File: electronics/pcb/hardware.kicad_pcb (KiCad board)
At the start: 4 copper layers, 59 x 53 mm, 145 parts, among them J1 Micro_SD_Card_Det_Hirose_DM3AT, J2 USB_A, J3 USB_A, J5 Conn_02x10_Odd_Even, U1 AS4C512M16D3L-12BIN, U2 A33, U3 TPS62095RGTR, U4 TPS62095RGTR, U5 TPS62095RGTR, U6 TPS62095RGTR, U7 AP131-25, Y1 24Mhz, Y2 32.768khz

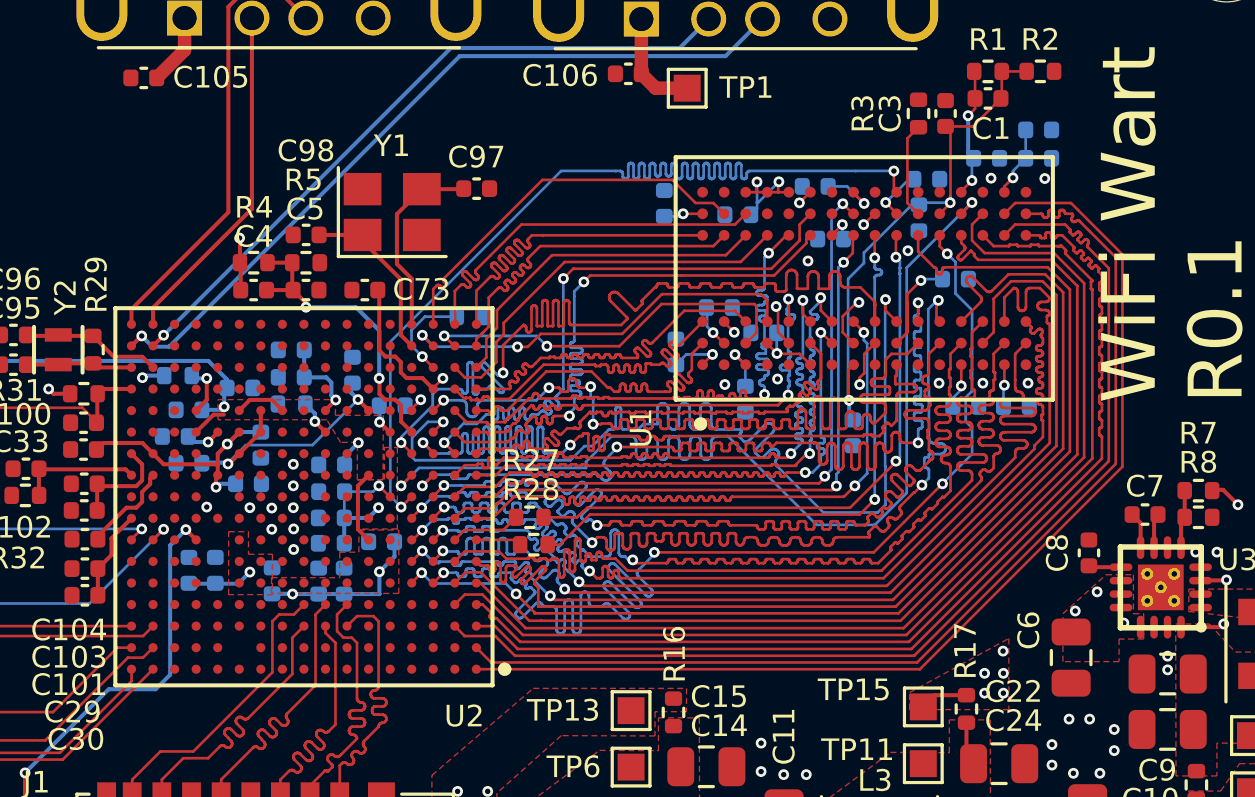
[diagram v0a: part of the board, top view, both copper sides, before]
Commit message: Working on the length matching
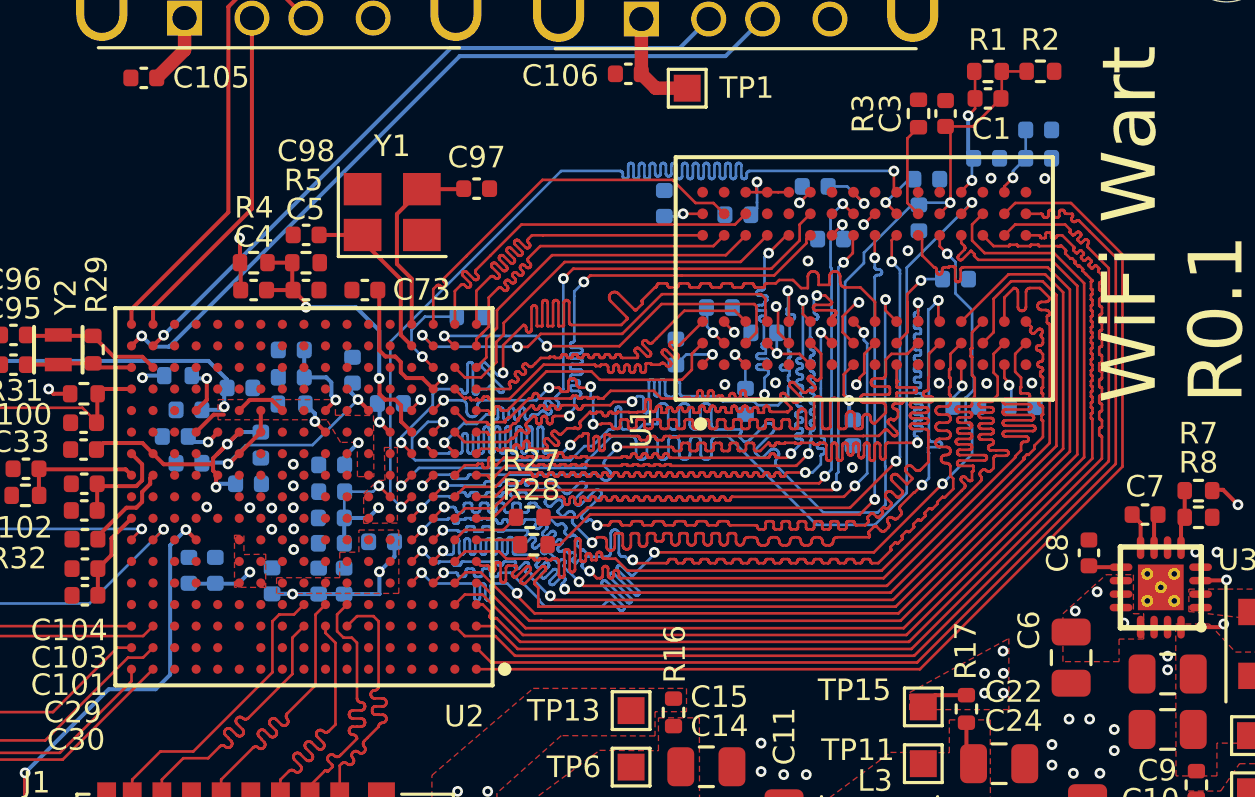
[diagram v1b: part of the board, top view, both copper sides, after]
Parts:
- moved C89 0.21 mm to (141.4, 105.6)
- moved C37 0.11 mm to (118.0, 105.5)
- moved C86 0.08 mm to (131.1, 105.4)
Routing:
- net adr15: track 48.5 -> 40.3 mm
- net d0: track 18.5 -> 24.1 mm
- net d2: track 19.7 -> 25.0 mm
- net d13: track 14.1 -> 10.4 mm
- net /ram/!RST: track 37.4 -> 40.3 mm
- net adr13: track 38.0 -> 40.8 mm
- net +1V1: track 32.8 -> 30.0 mm
- net adr2: track 38.0 -> 40.1 mm
- net adr7: track 37.3 -> 39.2 mm
- net /ram/!LDQS: track 22.3 -> 24.0 mm
- net /ram/!RAS: track 41.1 -> 39.4 mm
- net dba0: track 38.7 -> 40.3 mm
- net +1V35: track 68.9 -> 67.5 mm, vias 25 -> 24
- net /ram/ODT: track 38.9 -> 40.2 mm
- net adr10: track 39.5 -> 40.5 mm
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
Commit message: Length matching finished, again lol
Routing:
- net d13: track 10.4 -> 14.3 mm
- net /ram/!UDQS: track 13.4 -> 15.3 mm
- net /ram/UDQS: track 12.8 -> 14.7 mm
- net /ram/UDM: track 15.2 -> 14.4 mm
